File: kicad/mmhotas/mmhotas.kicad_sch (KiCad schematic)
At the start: 30 parts, among them J1 Conn_01x03_Male, J2 Conn_01x03_Male, J3 Conn_01x03_Male, J4 Conn_01x05_Male, J5 Conn_01x04_Male, J6 Conn_01x03_Male, J7 Conn_01x03_Male, J8 Conn_01x04_Male

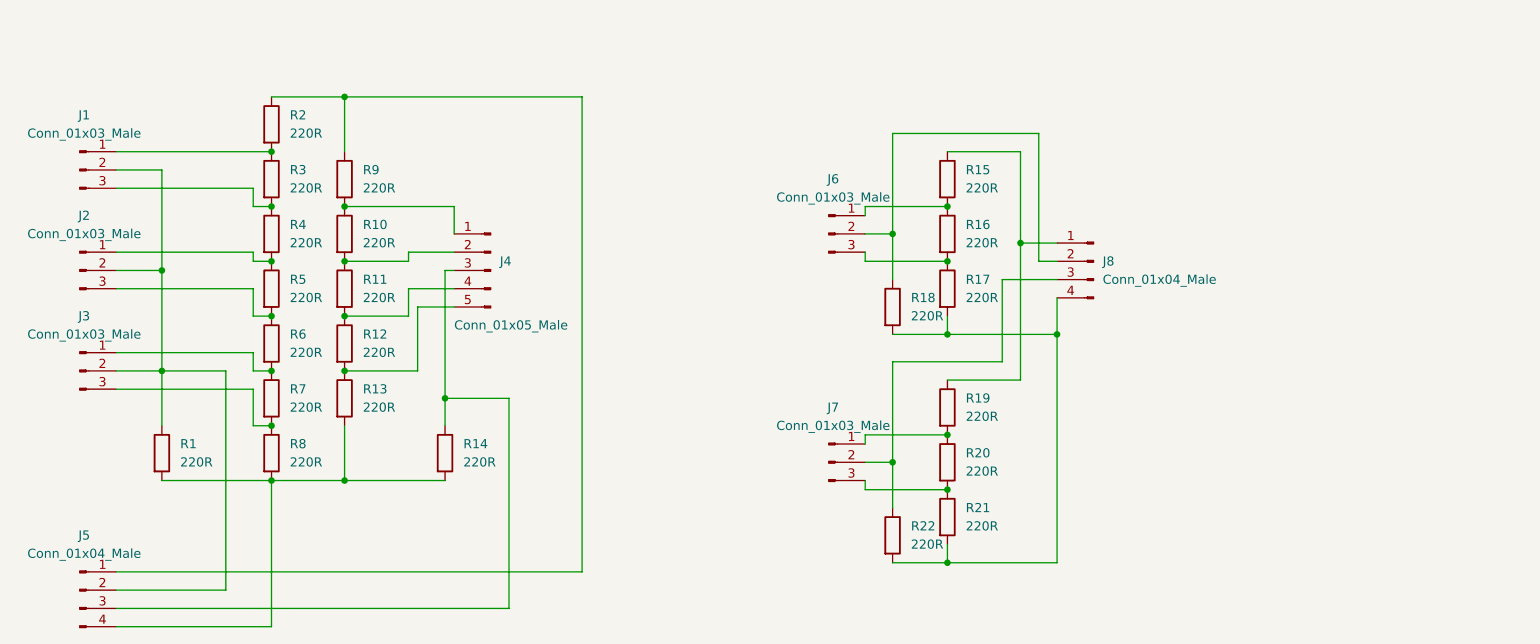
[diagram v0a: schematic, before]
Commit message: Designed connector board Backups removed
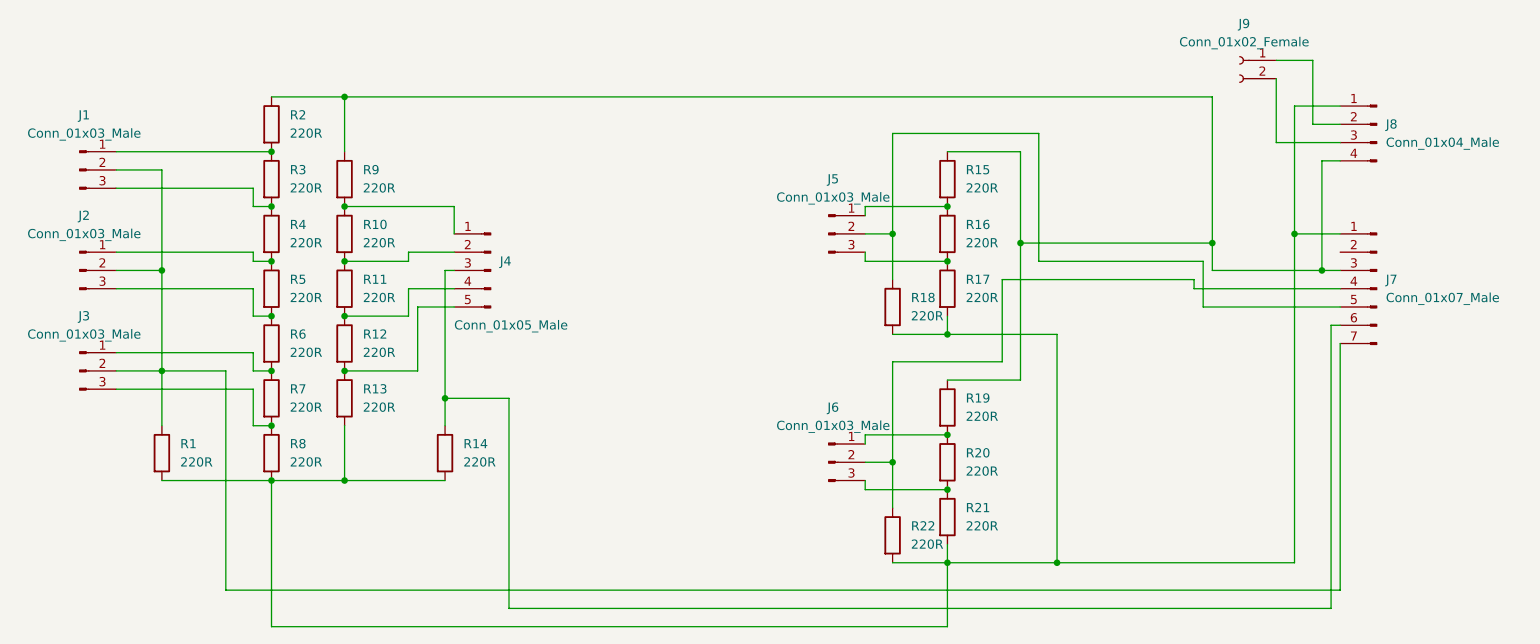
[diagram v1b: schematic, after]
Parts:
- removed J5: Conn_01x04_Male, Connector_PinHeader_2.54mm:PinHeader_1x04_P2.54mm_Vertical, symbol Connector:Conn_01x04_Male
- added J7: Conn_01x07_Male, Connector_PinHeader_2.54mm:PinHeader_1x07_P2.54mm_Vertical, symbol Connector:Conn_01x07_Male
- added J9: Conn_01x02_Female, Connector_PinSocket_2.54mm:PinSocket_1x02_P2.54mm_Vertical, symbol Connector:Conn_01x02_Female
- J8: footprint Connector_PinHeader_2.54mm:PinHeader_1x04_P2.54mm_Vertical -> Connector_PinHeader_2.54mm:PinHeader_1x04_P2.54mm_Horizontal
- renumbered J6 to J5, J7 to J6
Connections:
- net at R2.1, R9.1: now also J8.4 (Pin_4), R15.1, R19.1, J7.3 (Pin_3)
- net at R1.2, R13.2, R14.2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: now also J8.1 (Pin_1), R17.2, R18.2, R21.2, R22.2, J7.1 (Pin_1)
- net at J1.2 (Pin_2), J2.2 (Pin_2), J3.2 (Pin_2)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: now also J7.7 (Pin_7)
- net at J5.2 (Pin_2), R18.1: now also J7.5 (Pin_5); no longer J8.2 (Pin_2)
- net at J6.2 (Pin_2), R22.1: now also J7.4 (Pin_4); no longer J8.3 (Pin_3)
- net at J4.3 (Pin_3), R14.1: now also J7.6 (Pin_6)
- new net: J8.2 (Pin_2), J9.1 (Pin_1)
- new net: J8.3 (Pin_3), J9.2 (Pin_2)
